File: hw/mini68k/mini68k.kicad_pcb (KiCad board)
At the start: 2 copper layers, 147.3 x 100.3 mm, 37 parts, among them J1 Jack-DC, J2 6-bit input port, J3 8-bit output port, J4 FTDI header COM1, J5 FTDI header COM2, SW1 SW_SPDT, SW2 SW_Push, U1 HM62256BLP-7, U2 68008D, U3 L7805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

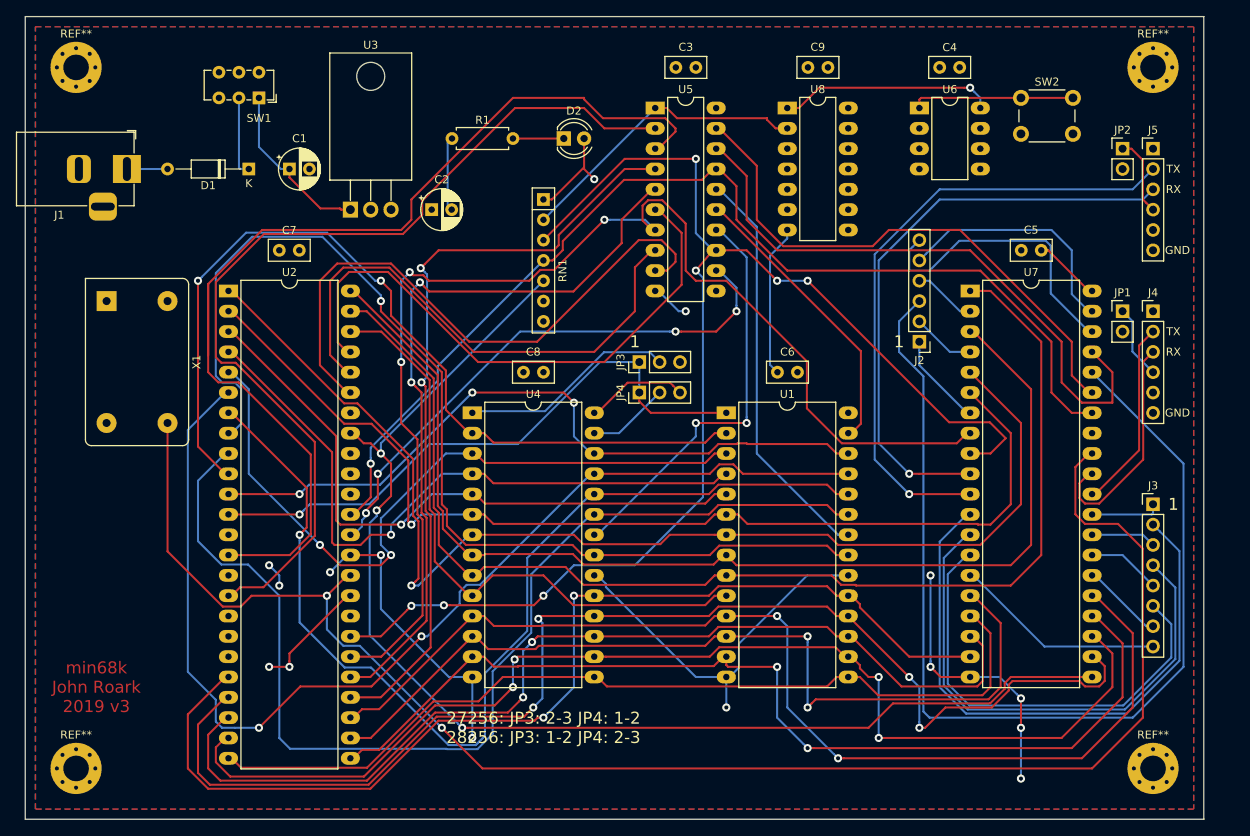
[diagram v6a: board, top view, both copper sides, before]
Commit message: seperate crystal for DUART
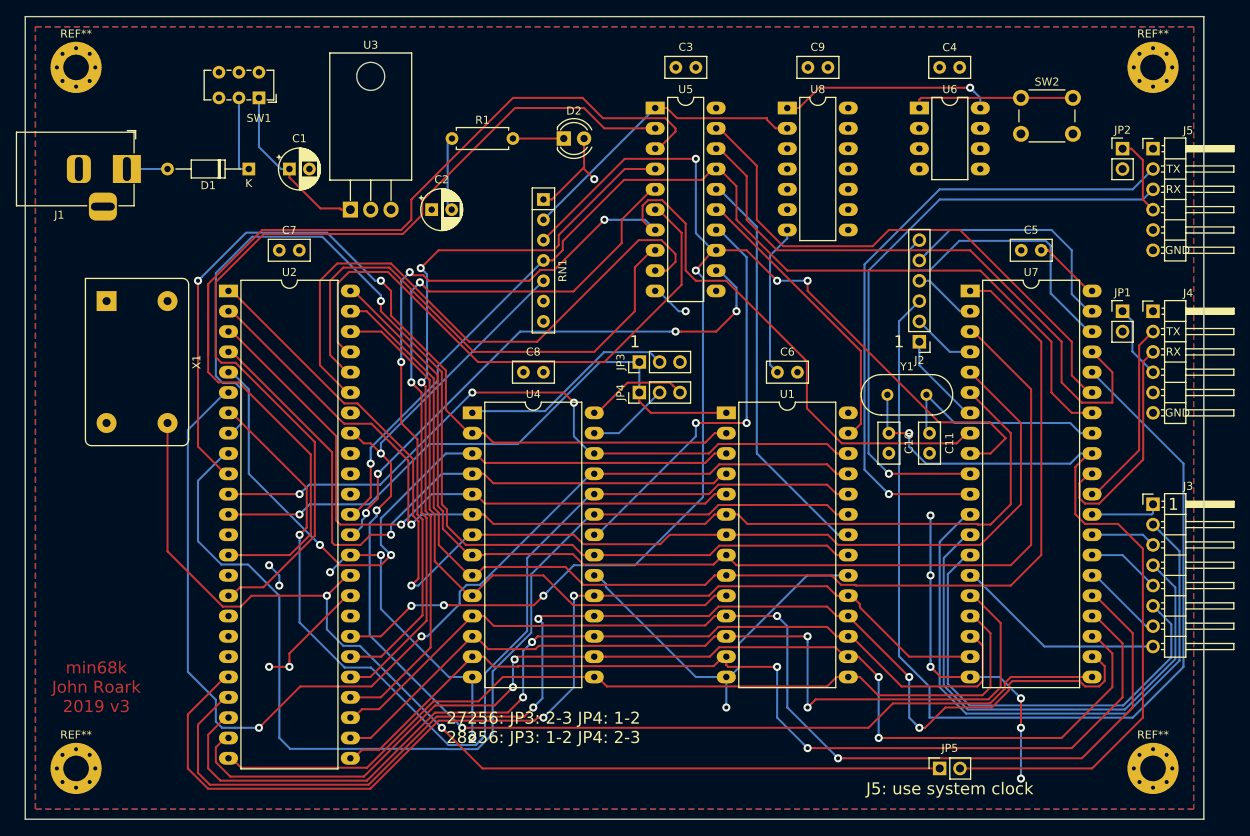
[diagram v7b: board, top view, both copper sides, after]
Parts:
- added C10: 5pf, Capacitor_THT:C_Disc_D5.0mm_W2.5mm_P2.50mm, F.Cu at (196.8, 115.6)
- added C11: 15pf, Capacitor_THT:C_Disc_D5.0mm_W2.5mm_P2.50mm, F.Cu at (201.9, 115.6)
- added JP5: Jumper, Connector_PinSocket_2.54mm:PinSocket_1x02_P2.54mm_Vertical, F.Cu at (203.2, 157.5)
- added Y1: 3.6864 Mhz, Crystal:Crystal_HC49-4H_Vertical, F.Cu at (196.7, 110.8)
- J3: footprint Connector_PinHeader_2.54mm:PinHeader_1x08_P2.54mm_Vertical -> Connector_PinHeader_2.54mm:PinHeader_1x08_P2.54mm_Horizontal
- J4, J5: footprint Connector_PinHeader_2.54mm:PinHeader_1x06_P2.54mm_Vertical -> Connector_PinHeader_2.54mm:PinHeader_1x06_P2.54mm_Horizontal
- RN1: value R_Network06 -> 1k
- X1: value TCXO-14 -> 8 Mhz
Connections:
- U7 pad 32: CLK -> X1
- U7 pad 33: Net-(U7-Pad33) -> X2
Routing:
- net X1: track 0.00 -> 98.9 mm, vias 0 -> 1
- net CLK: track 199.9 -> 131.8 mm
- net X2: track 0.00 -> 27.6 mm
- net GND: track 155.5 -> 163.0 mm, vias 12 -> 13
- net TX2: track 78.6 -> 81.1 mm
- net RX2: track 73.8 -> 76.4 mm
- net DTACK: track 170.8 -> 171.6 mm
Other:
- board text added: "J5: use system clock"
